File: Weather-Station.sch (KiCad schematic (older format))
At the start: 5 parts

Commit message: more in-progress work.....
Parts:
- added C?: 0.01uF, Capacitor_SMD:C_0805_2012Metric, symbol Device:C_Small
- added C?: 1000pF, Capacitor_SMD:C_0805_2012Metric, symbol Device:C_Small
- added C? (x2): 51pF, Capacitor_SMD:C_0805_2012Metric, symbol Device:C_Small
- added C? (x2): 300pF, Capacitor_SMD:C_0805_2012Metric, symbol Device:C_Small
- added C? (x3): 0.1uF, Capacitor_SMD:C_0805_2012Metric, symbol Device:C_Small
- added J?: Screw_Terminal_01x12, symbol Connector:Screw_Terminal_01x12
- added R? (x2): 10M, Resistor_SMD:R_0805_2012Metric, symbol Device:R_Small
- added R?: 52.3k, Resistor_SMD:R_0805_2012Metric, symbol Device:R_Small
- added R?: 154k, Resistor_SMD:R_0805_2012Metric, symbol Device:R_Small
- added R? (x2): 200R, Resistor_SMD:R_0805_2012Metric, symbol Device:R_Small
- added R?: 1k,1%, Resistor_SMD:R_0805_2012Metric, symbol Device:R_Small
- added R?: 1k, Resistor_SMD:R_0805_2012Metric, symbol Device:R_Small
- added R? (x8): 22R, Resistor_SMD:R_0805_2012Metric, symbol Device:R_Small
- added R?: 10k, Resistor_SMD:R_0805_2012Metric, symbol Device:R_Small
- added U?: SiT8918AE-13-33E-5.000000G, Oscillator:Oscillator_SMD_Abracon_ASDMB-4Pin_2.5x2.0mm, symbol SiT8918AE:SiT8918AE-13-33E-5.000000G
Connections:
- net labels added: CLK, COMPIN, LNAOUT, MISO, MOSI, PGAIN, PGAOUT, RTD1, RTD2, RX1, RX2, SCK, TDC1000CHSEL, TDC1000CSB, TDC1000EN, TDC1000RESET, TDC7200CSB, TDC7200EN, TDC7200INT, TRIGGER, TX1, TX2, VCOM, VDD
- wire segments 7 -> 106
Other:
- note added: "HP = 20.264kHz"
- note added: "LP = 59.668kHz"
- moved on the sheet: C?, U?

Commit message: more work.......
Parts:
- added BT?: 18650, Battery:BatteryHolder_Keystone_1042_1x18650, symbol Device:Battery_Cell
- added C? (x6): 1uF, Capacitor_SMD:C_0805_2012Metric, symbol Device:C_Small
- added C?: 0.01uF, Capacitor_SMD:C_0805_2012Metric, symbol Device:C_Small
- added C? (x2): 10uF, Capacitor_SMD:C_0805_2012Metric, symbol Device:C_Small
- added C?: 6.8pF, Capacitor_SMD:C_0805_2012Metric, symbol Device:C_Small
- added J?: PV IN, symbol Connector:Screw_Terminal_01x02
- added R?: 10k, Resistor_SMD:R_0805_2012Metric, symbol Device:R_Small
- added R?: 51.1k, Resistor_SMD:R_0805_2012Metric, symbol Device:R_Small
- added R?: 115k, Resistor_SMD:R_0805_2012Metric, symbol Device:R_Small
- added U?: MCP73812T-420I-OT, Package_TO_SOT_SMD:SOT-23-5, symbol Battery_Management:MCP73812T-420I-OT
- added U?: LP2985-33DBVR, Package_TO_SOT_SMD:SOT-23-5, symbol Regulator_Linear:LP2985-3.3
- added U?: LP2980IM5-ADJ, Package_TO_SOT_SMD:SOT-23-5, symbol Regulator_Linear:LP2980-ADJ
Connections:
- net labels added: +BATT
- wire segments 106 -> 151
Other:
- note added: "100mA\nCharge Rate"
- note added: "5.00MHz\nMEMS Oscillator"
- note added: "LP2980 Vout = 3.98V @ 50mA\nVout = 1.225+(1.225(Radj/51.5k))\nVdropout = 150mV so will drop out\nat 3.83V"
- note added: "LP2985 VIN(min) is approx 3.85V.\nShould be safe for 18650."
- moved on the sheet: C?, J?, R?, U?

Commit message: more work
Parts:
- removed C? (x2): 1uF, Capacitor_SMD:C_0805_2012Metric, symbol Device:C_Small
- removed C?: 10uF, Capacitor_SMD:C_0805_2012Metric, symbol Device:C_Small
- removed C?: 6.8pF, Capacitor_SMD:C_0805_2012Metric, symbol Device:C_Small
- removed R?: 51.1k, Resistor_SMD:R_0805_2012Metric, symbol Device:R_Small
- removed R?: 115k, Resistor_SMD:R_0805_2012Metric, symbol Device:R_Small
- removed U?: LP2980IM5-ADJ, Package_TO_SOT_SMD:SOT-23-5, symbol Regulator_Linear:LP2980-ADJ
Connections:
- net labels removed: VDD
- wire segments 151 -> 130
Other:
- note removed: "LP2980 Vout = 3.98V @ 50mA\nVout = 1.225+(1.225(Radj/51.5k))\nVdropout = 150mV so will drop out\nat 3.83V"
- moved on the sheet: C?

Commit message: Added VBAT monitor
added vbat monitor and changed vreg to low dropout type
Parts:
- removed U?: LP2985-33DBVR, Package_TO_SOT_SMD:SOT-23-5, symbol Regulator_Linear:LP2985-3.3
- added IC?: TPS3700DDCR, Package_TO_SOT_SMD:TSOT-23-6, symbol TPS3700DDCR:TPS3700DDCR
- added R?: 887k, Resistor_SMD:R_0805_2012Metric, symbol Device:R_Small
- added R?: 26.1k, Resistor_SMD:R_0805_2012Metric, symbol Device:R_Small
- added R?: 91k, Resistor_SMD:R_0805_2012Metric, symbol Device:R_Small
- added R?: 50k, Resistor_SMD:R_0805_2012Metric, symbol Device:R_Small
- added U?: Wemos_S2, symbol WemosS2:Wemos_S2
- added U?: TPS73633DBV, Package_TO_SOT_SMD:SOT-23-5, symbol Regulator_Linear:TPS73633DBV
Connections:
- net labels added: BATTOK
- wire segments 130 -> 161
- no-connect marks 0 -> 1
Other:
- note added: "TPS73633DBV VIN(min) is approx 3.375V. \nVdrop = 75mV."
- note added: "Vhigh = 4.4V approx.\nVlow = 3.375V approx."
- note removed: "LP2985 VIN(min) is approx 3.85V.\nShould be safe for 18650."
- moved on the sheet: C?, J?, R?, U?

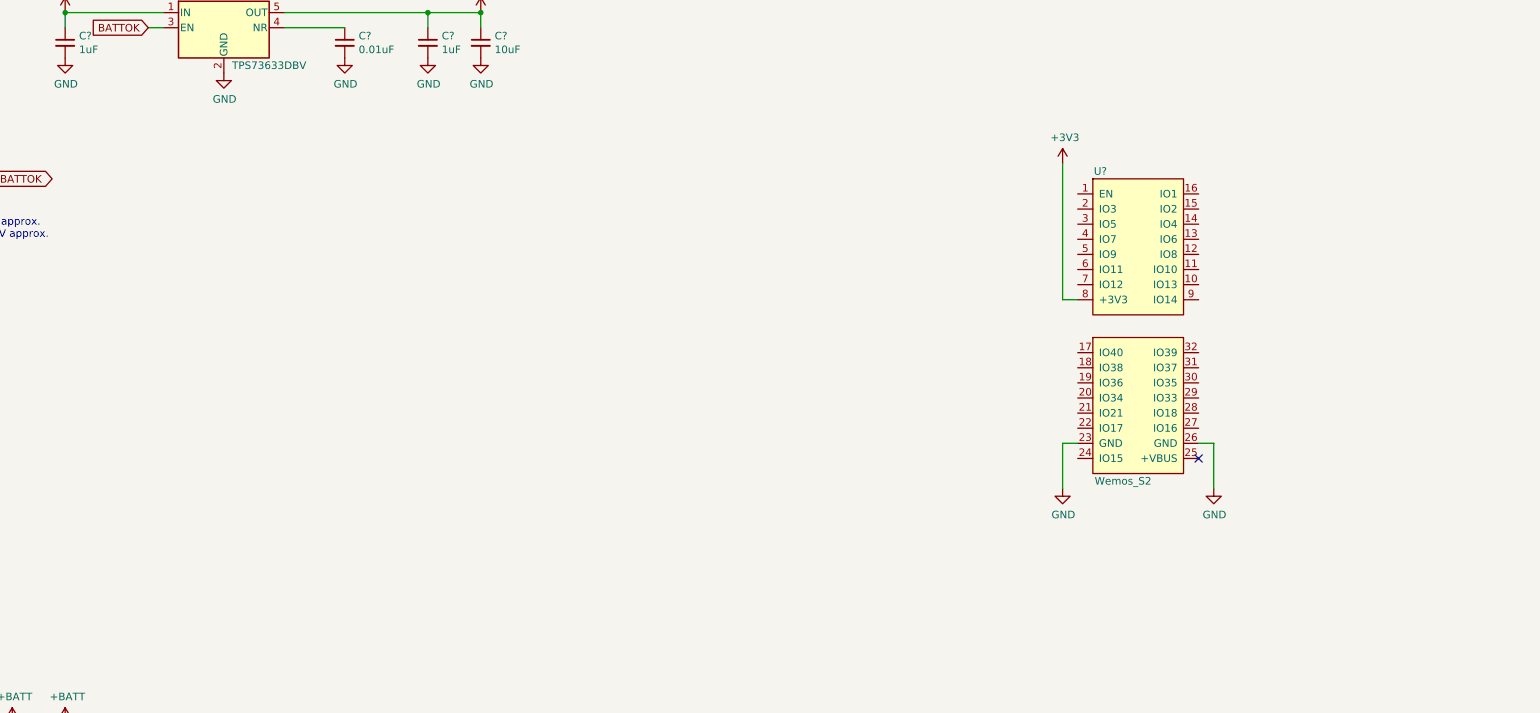
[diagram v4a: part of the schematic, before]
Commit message: Add lightning sensor interface
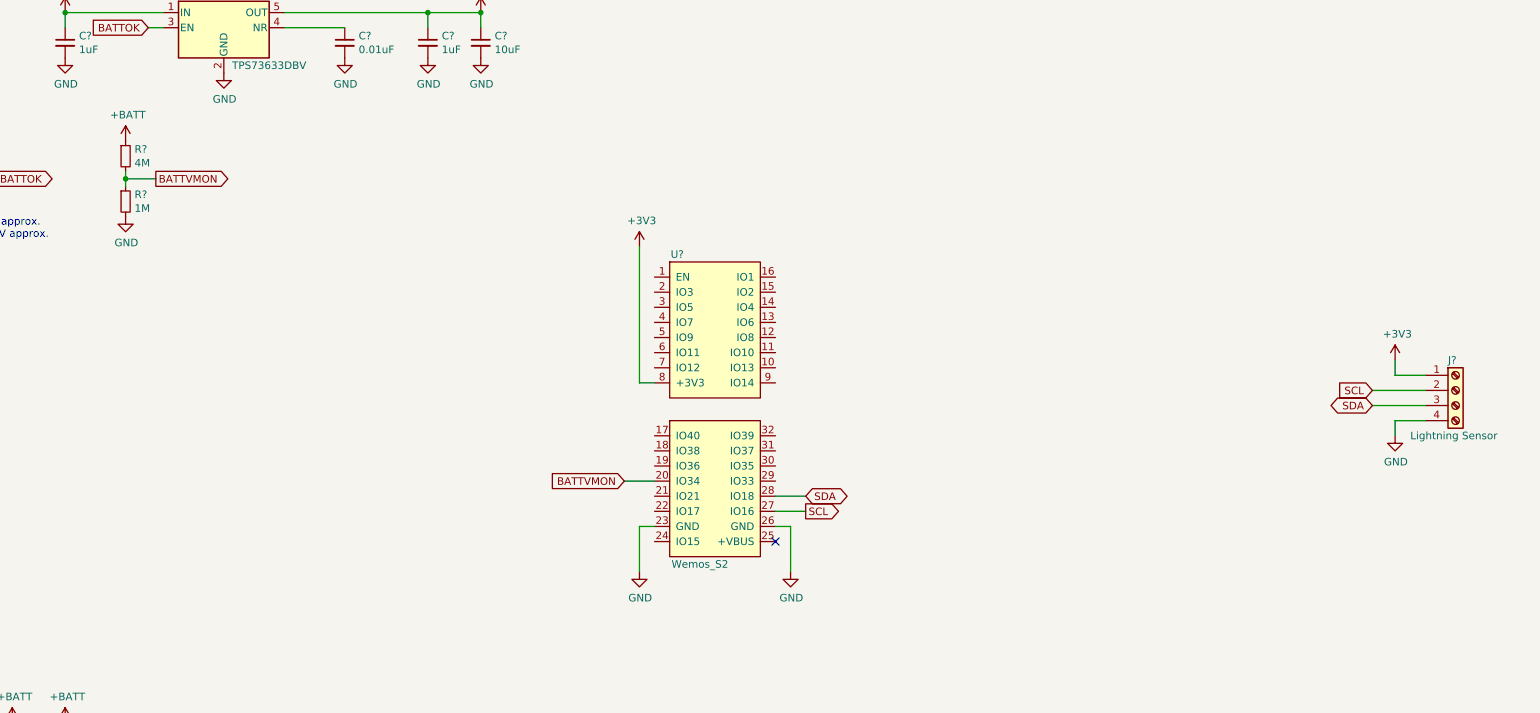
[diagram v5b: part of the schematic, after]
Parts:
- added J?: Lightning Sensor, symbol Connector:Screw_Terminal_01x04
- added R?: 4M, Resistor_SMD:R_0805_2012Metric, symbol Device:R_Small
- added R?: 1M, Resistor_SMD:R_0805_2012Metric, symbol Device:R_Small
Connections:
- net +3V3: now also J?.1 (Pin_1)
- net +BATT: now also R?.1
- net GND: now also J?.4 (Pin_4), R?.2
- net BATTVMON: now reaches U?.20 (IO34)
- net BATTVMON: now also R?.1, R?.2
- net SCL: now reaches U?.27 (IO16)
- net SCL: now also J?.2 (Pin_2)
- net SDA: now reaches U?.28 (IO18)
- net SDA: now also J?.3 (Pin_3)
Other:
- moved on the sheet: U?
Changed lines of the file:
@@
 L WemosS2:Wemos_S2 U?
 U 1 1 618E7311
-P 12200 2950
-F 0 "U?" H 12250 3000 50  0000 C CNN
-F 1 "Wemos_S2" H 12400 950 50  0000 C CNN
-F 2 "" H 12200 2900 50  0001 C CNN
-F 3 "" H 12200 2900 50  0001 C CNN
-	1    12200 2950
+P 9400 3500
+F 0 "U?" H 9450 3550 50  0000 C CNN
+F 1 "Wemos_S2" H 9600 1500 50  0000 C CNN
+F 2 "" H 9400 3450 50  0001 C CNN
+F 3 "" H 9400 3450 50  0001 C CNN
+	1    9400 3500
 	1    0    0    -1
 $EndComp
@@
 L power:+3V3 #PWR?
 U 1 1 61A53F67
-P 12000 2850
-F 0 "#PWR?" H 12000 2700 50  0001 C CNN
-F 1 "+3V3" H 12015 3023 50  0000 C CNN
-F 2 "" H 12000 2850 50  0001 C CNN
-F 3 "" H 12000 2850 50  0001 C CNN
-	1    12000 2850
-	1    0    0    -1
-$EndComp
-NoConn ~ 12900 4800
-Wire Wire Line
-	12000 2850 12000 3750
-Wire Wire Line
-	12000 3750 12100 3750
+P 9200 3400
+F 0 "#PWR?" H 9200 3250 50  0001 C CNN
+F 1 "+3V3" H 9215 3573 50  0000 C CNN
+F 2 "" H 9200 3400 50  0001 C CNN
+F 3 "" H 9200 3400 50  0001 C CNN
+	1    9200 3400
+	1    0    0    -1
+$EndComp
+NoConn ~ 10100 5350
+Wire Wire Line
+	9200 3400 9200 4300
+Wire Wire Line
+	9200 4300 9300 4300
 $Comp
 L power:GND #PWR?
 U 1 1 61A64F93
-P 12000 5000
-F 0 "#PWR?" H 12000 4750 50  0001 C CNN
-F 1 "GND" H 12005 4827 50  0000 C CNN
-F 2 "" H 12000 5000 50  0001 C CNN
-F 3 "" H 12000 5000 50  0001 C CNN
-	1    12000 5000
+P 9200 5550
+F 0 "#PWR?" H 9200 5300 50  0001 C CNN
+F 1 "GND" H 9205 5377 50  0000 C CNN
+F 2 "" H 9200 5550 50  0001 C CNN
+F 3 "" H 9200 5550 50  0001 C CNN
+	1    9200 5550
 	1    0    0    -1
 $EndComp
@@
 L power:GND #PWR?
 U 1 1 61A657A2
-P 13000 5000
-F 0 "#PWR?" H 13000 4750 50  0001 C CNN
-F 1 "GND" H 13005 4827 50  0000 C CNN
-F 2 "" H 13000 5000 50  0001 C CNN
-F 3 "" H 13000 5000 50  0001 C CNN
-	1    13000 5000
-	1    0    0    -1
-$EndComp
-Wire Wire Line
-	13000 5000 13000 4700
-Wire Wire Line
-	13000 4700 12900 4700
-Wire Wire Line
-	12000 5000 12000 4700
-Wire Wire Line
-	12000 4700 12100 4700
+P 10200 5550
+F 0 "#PWR?" H 10200 5300 50  0001 C CNN
+F 1 "GND" H 10205 5377 50  0000 C CNN
+F 2 "" H 10200 5550 50  0001 C CNN
+F 3 "" H 10200 5550 50  0001 C CNN
+	1    10200 5550
+	1    0    0    -1
+$EndComp
+Wire Wire Line
+	10200 5550 10200 5250
+Wire Wire Line
+	10200 5250 10100 5250
+Wire Wire Line
+	9200 5550 9200 5250
+Wire Wire Line
+	9200 5250 9300 5250
 Text Notes 4500 3350 0    50   ~ 0
 Vhigh = 4.4V approx.\nVlow = 3.375V approx.
+Text GLabel 9100 4950 0    50   Input ~ 0
+BATTVMON
+Wire Wire Line
+	9300 4950 9100 4950
+Text GLabel 6000 2950 2    50   Output ~ 0
+BATTVMON
+$Comp
+L Device:R_Small R?
+U 1 1 61A81642
+P 5800 2800
+F 0 "R?" H 5859 2846 50  0000 L CNN
+F 1 "4M" H 5859 2755 50  0000 L CNN
+F 2 "Resistor_SMD:R_0805_2012Metric" H 5800 2800 50  0001 C CNN
+F 3 "~" H 5800 2800 50  0001 C CNN
+	1    5800 2800
+	1    0    0    -1
+$EndComp
+$Comp
+L Device:R_Small R?
+U 1 1 61A817FF
+P 5800 3100
+F 0 "R?" H 5859 3146 50  0000 L CNN
+F 1 "1M" H 5859 3055 50  0000 L CNN
+F 2 "Resistor_SMD:R_0805_2012Metric" H 5800 3100 50  0001 C CNN
+F 3 "~" H 5800 3100 50  0001 C CNN
+	1    5800 3100
+	1    0    0    -1
+$EndComp
+$Comp
+L power:GND #PWR?
+U 1 1 61A81AF5
+P 5800 3200
+F 0 "#PWR?" H 5800 2950 50  0001 C CNN
+F 1 "GND" H 5805 3027 50  0000 C CNN
+F 2 "" H 5800 3200 50  0001 C CNN
+F 3 "" H 5800 3200 50  0001 C CNN
+	1    5800 3200
+	1    0    0    -1
+$EndComp
+$Comp
+L power:+BATT #PWR?
+U 1 1 61A8AF03
+P 5800 2700
+F 0 "#PWR?" H 5800 2550 50  0001 C CNN
+F 1 "+BATT" H 5815 2873 50  0000 C CNN
+F 2 "" H 5800 2700 50  0001 C CNN
+F 3 "" H 5800 2700 50  0001 C CNN
+	1    5800 2700
+	1    0    0    -1
+$EndComp
+Wire Wire Line
+	5800 2900 5800 2950
+Connection ~ 5800 2950
+Wire Wire Line
+	5800 2950 5800 3000
+Wire Wire Line
+	5800 2950 6000 2950
+Text GLabel 10300 5050 2    50   BiDi ~ 0
+SDA
+Wire Wire Line
+	10300 5050 10100 5050
+Text GLabel 10300 5150 2    50   Output ~ 0
+SCL
+Wire Wire Line
+	10300 5150 10100 5150
+Text GLabel 14050 4450 0    50   BiDi ~ 0
+SDA
+Text GLabel 14050 4350 0    50   Input ~ 0
+SCL
+$Comp
+L power:GND #PWR?
+U 1 1 61AD0840
+P 14200 4650
+F 0 "#PWR?" H 14200 4400 50  0001 C CNN
+F 1 "GND" H 14205 4477 50  0000 C CNN
+F 2 "" H 14200 4650 50  0001 C CNN
+F 3 "" H 14200 4650 50  0001 C CNN
+	1    14200 4650
+	1    0    0    -1
+$EndComp
+$Comp
+L power:+3V3 #PWR?
+U 1 1 61AD0C5F
+P 14200 4150
+F 0 "#PWR?" H 14200 4000 50  0001 C CNN
+F 1 "+3V3" H 14215 4323 50  0000 C CNN
+F 2 "" H 14200 4150 50  0001 C CNN
+F 3 "" H 14200 4150 50  0001 C CNN
+	1    14200 4150
+	1    0    0    -1
+$EndComp
+$Comp
+L Connector:Screw_Terminal_01x04 J?
+U 1 1 61AD21F2
+P 14600 4350
+F 0 "J?" H 14550 4550 50  0000 L CNN
+F 1 "Lightning Sensor" H 14300 4050 50  0000 L CNN
+F 2 "" H 14600 4350 50  0001 C CNN
+F 3 "~" H 14600 4350 50  0001 C CNN
+	1    14600 4350
+	1    0    0    -1
+$EndComp
+Wire Wire Line
+	14400 4250 14200 4250
+Wire Wire Line
+	14200 4250 14200 4150
+Wire Wire Line
+	14400 4350 14050 4350
+Wire Wire Line
+	14050 4450 14400 4450
+Wire Wire Line
+	14400 4550 14200 4550
+Wire Wire Line
+	14200 4550 14200 4650
 $EndSCHEMATC
